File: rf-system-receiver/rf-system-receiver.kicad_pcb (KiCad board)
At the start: 4 copper layers, 53.3 x 51 mm, 55 parts, among them IC1 nRF905, J1 USB_B_Micro, J2 CONREVSMA001-G, J3 SWD, Q1 MMBT9013, SW1 SW_Push, U1 STM32F103C8Tx, U2 AMS1117-3.3, X1 16MHZ, X2 16MHZ

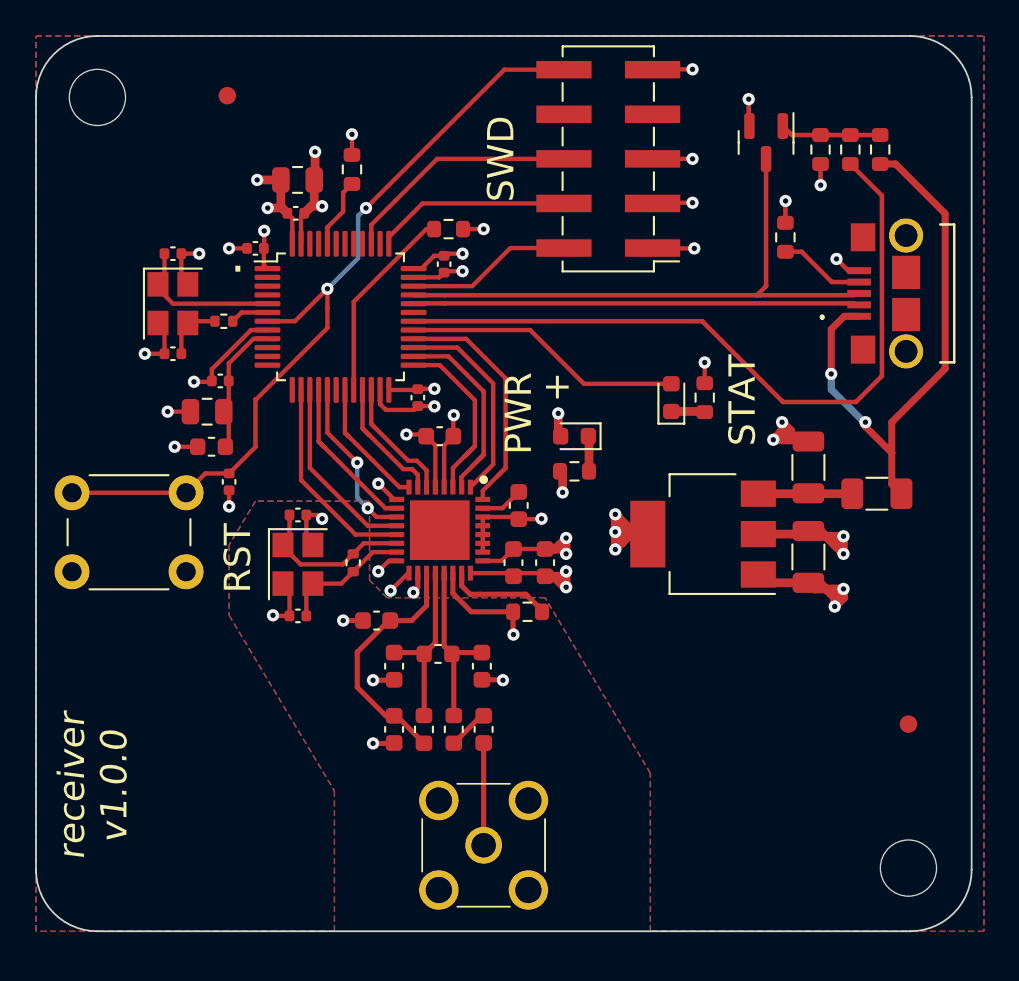
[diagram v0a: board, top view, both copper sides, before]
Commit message: add silkscreen, fiducials and tooling holes
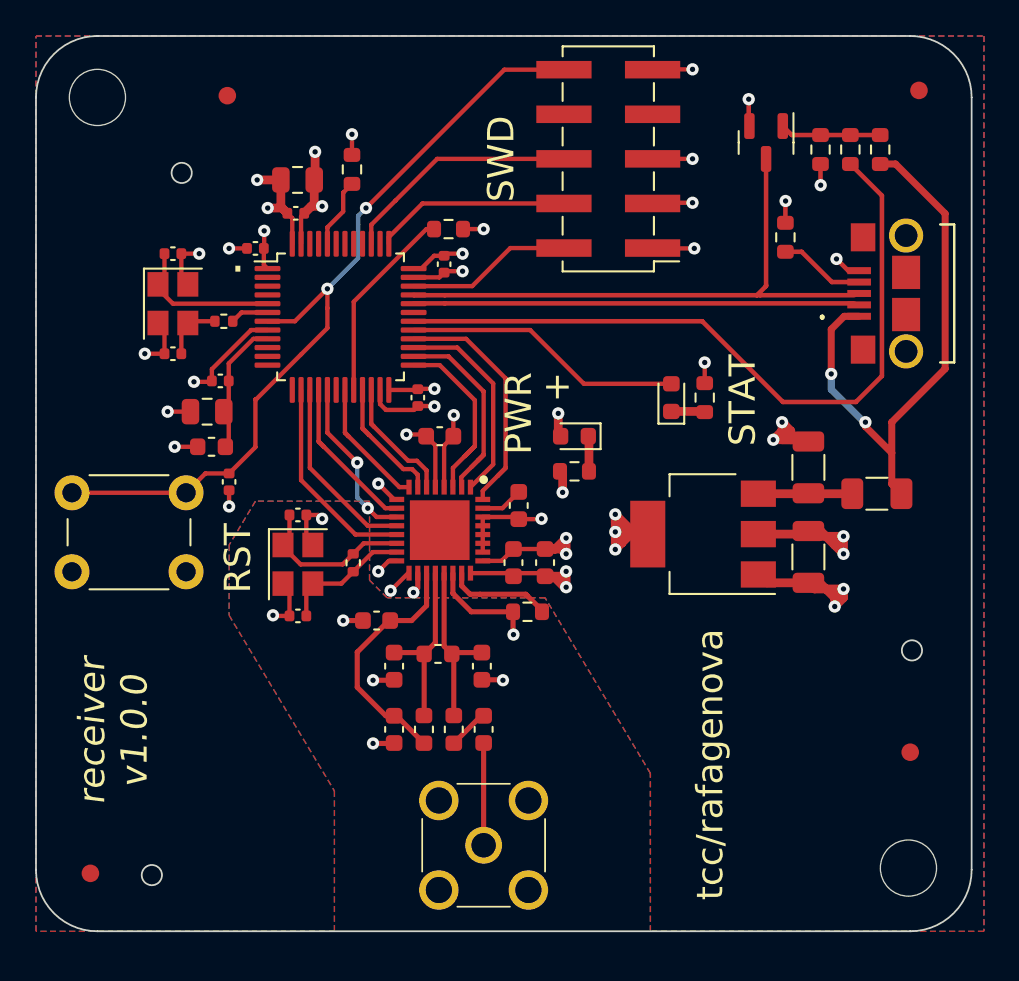
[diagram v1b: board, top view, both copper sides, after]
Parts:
- added FID3: Fiducial, Fiducial:Fiducial_1mm_Mask2mm, F.Cu at (119.1, 83.7)
- added FID4: Fiducial, Fiducial:Fiducial_1mm_Mask2mm, F.Cu at (166.3, 39.1)
- moved FID2 1.60 mm to (165.8, 76.8)
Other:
- outline, holes or cut-outs redrawn
- board text added: "tcc/rafagenova"
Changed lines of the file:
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@@
     )
+  )
+  (footprint "Fiducial:Fiducial_1mm_Mask2mm" (layer "F.Cu")
+    (at 166.3 39.1)
+    (descr "Circular Fiducial, 1mm bare copper, 2mm soldermask opening (Level A)")
+    (tags "fiducial")
+    (property "Sheetfile" "rf-system-receiver.kicad_sch")
+    (property "Sheetname" "")
+    (attr smd)
+    (fp_text reference "FID4" (at 0 -2) (layer "F.Fab")
+      (effects (font (size 1 1) (thickness 0.15)))
+    )
+    (fp_text value "Fiducial" (at 0 2) (layer "F.Fab")
+      (effects (font (size 1 1) (thickness 0.15)))
+    )
+    (fp_text user "${REFERENCE}" (at 0 0) (layer "F.Fab")
+      (effects (font (size 0.4 0.4) (thickness 0.06)))
+    )
+    (fp_circle (center 0 0) (end 1.25 0) (layer "F.CrtYd") (width 0.05) (fill none))
+    (fp_circle (center 0 0) (end 1 0) (layer "F.Fab") (width 0.1) (fill none))
+    (pad "" smd circle (at 0 0) (size 1 1) (layers "F.Cu" "F.Mask")
+      (solder_mask_margin 0.5) (clearance 0.5))
   )
   (footprint "Connector_PinHeader_2.54mm:PinHeader_2x05_P2.54mm_Vertical_SMD" (layer "F.Cu")
@@
   )
   (footprint "Fiducial:Fiducial_1mm_Mask2mm" (layer "F.Cu")
-    (at 165.7 75.2)
+    (at 165.8 76.8)
     (descr "Circular Fiducial, 1mm bare copper, 2mm soldermask opening (Level A)")
     (tags "fiducial")
@@
     )
   )
+  (footprint "Fiducial:Fiducial_1mm_Mask2mm" (layer "F.Cu")
+    (at 119.1 83.7)
+    (descr "Circular Fiducial, 1mm bare copper, 2mm soldermask opening (Level A)")
+    (tags "fiducial")
+    (property "Sheetfile" "rf-system-receiver.kicad_sch")
+    (property "Sheetname" "")
+    (attr smd)
+    (fp_text reference "FID3" (at 0 -2) (layer "F.Fab")
+      (effects (font (size 1 1) (thickness 0.15)))
+    )
+    (fp_text value "Fiducial" (at 0 2) (layer "F.Fab")
+      (effects (font (size 1 1) (thickness 0.15)))
+    )
+    (fp_text user "${REFERENCE}" (at 0 0) (layer "F.Fab")
+      (effects (font (size 0.4 0.4) (thickness 0.06)))
+    )
+    (fp_circle (center 0 0) (end 1.25 0) (layer "F.CrtYd") (width 0.05) (fill none))
+    (fp_circle (center 0 0) (end 1 0) (layer "F.Fab") (width 0.1) (fill none))
+    (pad "" smd circle (at 0 0) (size 1 1) (layers "F.Cu" "F.Mask")
+      (solder_mask_margin 0.5) (clearance 0.5))
+  )
   (footprint "Capacitor_SMD:C_0805_2012Metric" (layer "F.Cu")
     (at 125.75 57.4 180)
@@
   )
   (gr_line (start 119.5 87) (end 165.8 87) (layer "Edge.Cuts") (width 0.1))
+  (gr_circle (center 124.3 43.8) (end 124.876 43.8) (layer "Edge.Cuts") (width 0.1) (fill none))
   (gr_arc (start 116 39.5) (mid 117.025126 37.025126) (end 119.5 36) (layer "Edge.Cuts") (width 0.1))
+  (gr_circle (center 122.6 83.8) (end 123.176 83.8) (layer "Edge.Cuts") (width 0.1) (fill none))
   (gr_line (start 116 39.5) (end 116 83.5) (layer "Edge.Cuts") (width 0.1))
   (gr_arc (start 119.5 87) (mid 117.025126 85.974874) (end 116 83.5) (layer "Edge.Cuts") (width 0.1))
   (gr_arc (start 165.8 36) (mid 168.274874 37.025126) (end 169.3 39.5) (layer "Edge.Cuts") (width 0.1))
+  (gr_circle (center 165.9 71) (end 166.476 71) (layer "Edge.Cuts") (width 0.1) (fill none))
   (gr_line (start 165.8 36) (end 119.5 36) (layer "Edge.Cuts") (width 0.1))
   (gr_arc (start 169.3 83.5) (mid 168.274874 85.974874) (end 165.8 87) (layer "Edge.Cuts") (width 0.1))
@@
     (effects (font (size 1.5 1.5) (thickness 0.3)))
   )
-  (gr_text "receiver\nv1.0.0" (at 119.25 78.75 90) (layer "F.SilkS")
+  (gr_text "receiver\nv1.0.0" (at 120.4 75.6 90) (layer "F.SilkS")
     (effects (font (size 1.5 1.5) (thickness 0.3) italic))
   )
@@
     (effects (font (size 1.5 1.5) (thickness 0.3)))
   )
+  (gr_text "tcc/rafagenova" (at 154.4 77.5 90) (layer "F.SilkS")
+    (effects (font (size 1.5 1.5) (thickness 0.3)))
+  )

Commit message: adding LCSC Part # and small PCB modifs
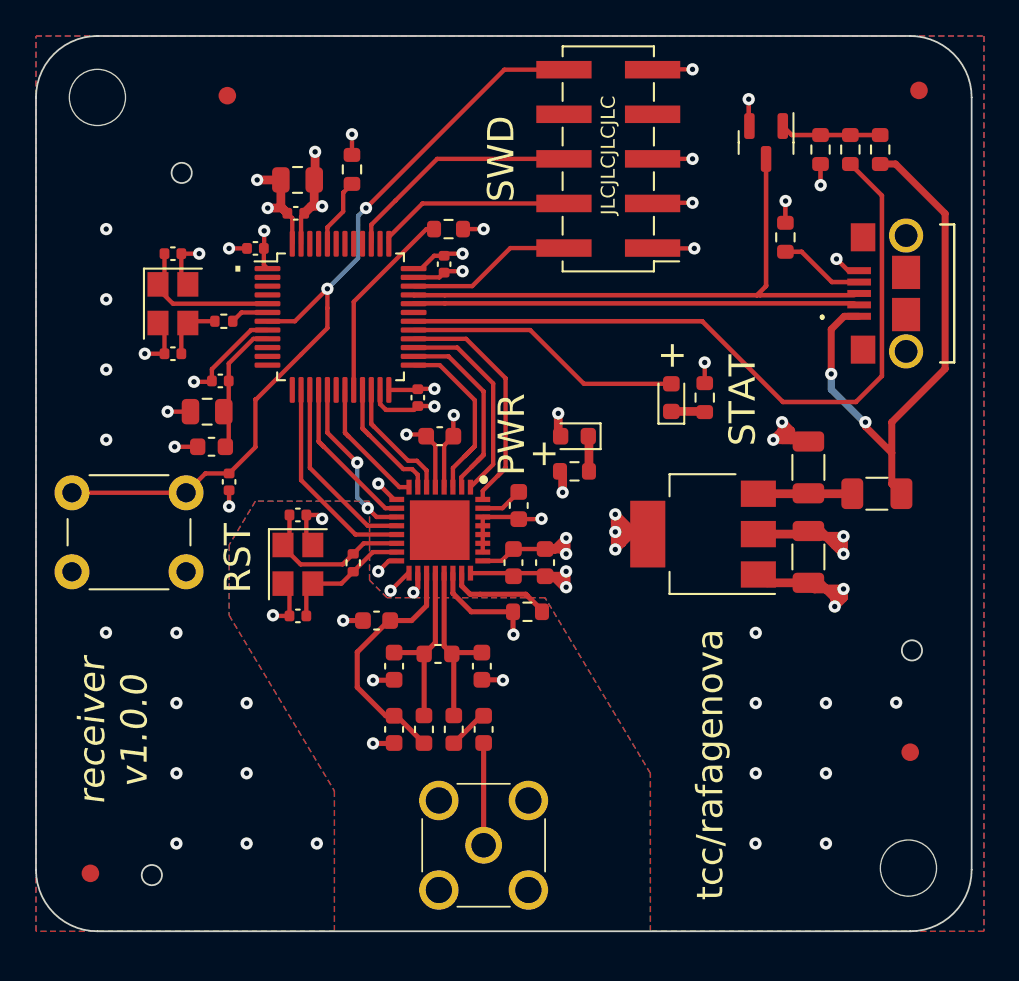
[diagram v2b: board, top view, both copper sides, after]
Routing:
- net GND: vias 38 -> 59
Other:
- board text added: "JLCJLCJLCJLC"
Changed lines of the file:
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@@
       (outputformat 1)
       (mirror false)
-      (drillshape 1)
+      (drillshape 0)
       (scaleselection 1)
-      (outputdirectory "")
+      (outputdirectory "gerber/")
     )
   )
@@
     (fp_line (start -1.6 0.8) (end -1.6 -0.8) (layer "F.Fab") (width 0.1))
     (fp_line (start -1.6 -0.8) (end 1.6 -0.8) (layer "F.Fab") (width 0.1))
-    (pad "1" smd roundrect (at -1.475 0 270) (size 1.15 1.8) (layers "F.Cu" "F.Paste" "F.Mask") (roundrect_rratio 0.217391)
+    (pad "1" smd roundrect (at -1.475 0 270) (size 1.15 1.8) (layers "F.Cu" "F.Paste" "F.Mask") (roundrect_rratio 0.2173913043)
       (net 2 "+3V3") (pintype "passive"))
-    (pad "2" smd roundrect (at 1.475 0 270) (size 1.15 1.8) (layers "F.Cu" "F.Paste" "F.Mask") (roundrect_rratio 0.217391)
+    (pad "2" smd roundrect (at 1.475 0 270) (size 1.15 1.8) (layers "F.Cu" "F.Paste" "F.Mask") (roundrect_rratio 0.2173913043)
       (net 1 "GND") (pintype "passive"))
     (model "${KICAD6_3DMODEL_DIR}/Capacitor_SMD.3dshapes/C_1206_3216Metric.wrl"
@@
     (fp_line (start -1.6 0.8) (end -1.6 -0.8) (layer "F.Fab") (width 0.1))
     (fp_line (start 1.6 -0.8) (end 1.6 0.8) (layer "F.Fab") (width 0.1))
-    (pad "1" smd roundrect (at -1.475 0 90) (size 1.15 1.8) (layers "F.Cu" "F.Paste" "F.Mask") (roundrect_rratio 0.217391)
+    (pad "1" smd roundrect (at -1.475 0 90) (size 1.15 1.8) (layers "F.Cu" "F.Paste" "F.Mask") (roundrect_rratio 0.2173913043)
       (net 3 "Net-(C2-Pad1)") (pintype "passive"))
-    (pad "2" smd roundrect (at 1.475 0 90) (size 1.15 1.8) (layers "F.Cu" "F.Paste" "F.Mask") (roundrect_rratio 0.217391)
+    (pad "2" smd roundrect (at 1.475 0 90) (size 1.15 1.8) (layers "F.Cu" "F.Paste" "F.Mask") (roundrect_rratio 0.2173913043)
       (net 1 "GND") (pintype "passive"))
     (model "${KICAD6_3DMODEL_DIR}/Capacitor_SMD.3dshapes/C_1206_3216Metric.wrl"
@@
   (gr_arc (start 169.3 83.5) (mid 168.274874 85.974874) (end 165.8 87) (layer "Edge.Cuts") (width 0.1))
   (gr_line (start 169.3 83.5) (end 169.3 39.5) (layer "Edge.Cuts") (width 0.1))
-  (gr_text "PWR" (at 143.5 57.5 90) (layer "F.SilkS")
+  (gr_text "+" (at 152.3 54.2 270) (layer "F.SilkS")
+    (effects (font (size 1.5 1.5) (thickness 0.3)))
+  )
+  (gr_text "PWR" (at 143.1 58.7 90) (layer "F.SilkS")
     (effects (font (size 1.5 1.5) (thickness 0.3)))
   )
@@
     (effects (font (size 1.5 1.5) (thickness 0.3)))
   )
-  (gr_text "+" (at 145.75 56 270) (layer "F.SilkS")
+  (gr_text "+" (at 145 59.8 270) (layer "F.SilkS")
     (effects (font (size 1.5 1.5) (thickness 0.3)))
+  )
+  (gr_text "JLCJLCJLCJLC" (at 148.6 42.8 90) (layer "F.SilkS")
+    (effects (font (size 0.8 0.8) (thickness 0.15)))
   )
   (gr_text "tcc/rafagenova" (at 154.4 77.5 90) (layer "F.SilkS")
@@
   (segment (start 158.69 45.41) (end 158.7 45.4) (width 0.261112) (layer "F.Cu") (net 1))
   (via (at 137.1 58.7) (size 0.7) (drill 0.3) (layers "F.Cu" "B.Cu") (free) (net 1))
+  (via (at 120 55) (size 0.7) (drill 0.3) (layers "F.Cu" "B.Cu") (free) (net 1))
   (via (at 146 62) (size 0.7) (drill 0.3) (layers "F.Cu" "B.Cu") (free) (net 1))
   (via (at 158.5 58) (size 0.7) (drill 0.3) (layers "F.Cu" "B.Cu") (free) (net 1))
@@
   (via (at 132.3 63.5) (size 0.7) (drill 0.3) (layers "F.Cu" "B.Cu") (free) (net 1))
   (via (at 153.4 45.5) (size 0.7) (drill 0.3) (layers "F.Cu" "B.Cu") (net 1))
+  (via (at 157 70) (size 0.7) (drill 0.3) (layers "F.Cu" "B.Cu") (free) (net 1))
+  (via (at 123.999999 82) (size 0.7) (drill 0.3) (layers "F.Cu" "B.Cu") (free) (net 1))
   (via (at 140.3 49.4) (size 0.7) (drill 0.3) (layers "F.Cu" "B.Cu") (free) (net 1))
   (via (at 146.2 66.5) (size 0.7) (drill 0.3) (layers "F.Cu" "B.Cu") (free) (net 1))
   (via (at 129.5 69) (size 0.7) (drill 0.3) (layers "F.Cu" "B.Cu") (free) (net 1))
+  (via (at 120 47) (size 0.7) (drill 0.3) (layers "F.Cu" "B.Cu") (free) (net 1))
   (via (at 137.5 67.7) (size 0.7) (drill 0.3) (layers "F.Cu" "B.Cu") (free) (net 1))
   (via (at 133.5 69.3) (size 0.7) (drill 0.3) (layers "F.Cu" "B.Cu") (free) (net 1))
   (via (at 160.7 44.5) (size 0.7) (drill 0.3) (layers "F.Cu" "B.Cu") (free) (net 1))
   (via (at 125.3 48.4) (size 0.7) (drill 0.3) (layers "F.Cu" "B.Cu") (free) (net 1))
+  (via (at 157 78) (size 0.7) (drill 0.3) (layers "F.Cu" "B.Cu") (free) (net 1))
   (via (at 122.2 54.1) (size 0.7) (drill 0.3) (layers "F.Cu" "B.Cu") (free) (net 1))
+  (via (at 157 74) (size 0.7) (drill 0.3) (layers "F.Cu" "B.Cu") (free) (net 1))
+  (via (at 120 59) (size 0.7) (drill 0.3) (layers "F.Cu" "B.Cu") (free) (net 1))
   (via (at 135.5 66.5) (size 0.7) (drill 0.3) (layers "F.Cu" "B.Cu") (free) (net 1))
   (via (at 134 41.6) (size 0.7) (drill 0.3) (layers "F.Cu" "B.Cu") (free) (net 1))
   (via (at 162 67.5) (size 0.7) (drill 0.3) (layers "F.Cu" "B.Cu") (free) (net 1))
+  (via (at 123.999055 74) (size 0.7) (drill 0.3) (layers "F.Cu" "B.Cu") (free) (net 1))
+  (via (at 120 51) (size 0.7) (drill 0.3) (layers "F.Cu" "B.Cu") (free) (net 1))
+  (via (at 124 78) (size 0.7) (drill 0.3) (layers "F.Cu" "B.Cu") (free) (net 1))
+  (via (at 161 82) (size 0.7) (drill 0.3) (layers "F.Cu" "B.Cu") (free) (net 1))
+  (via (at 156.987016 82) (size 0.7) (drill 0.3) (layers "F.Cu" "B.Cu") (free) (net 1))
+  (via (at 161 74) (size 0.7) (drill 0.3) (layers "F.Cu" "B.Cu") (free) (net 1))
   (via (at 143.2 70.1) (size 0.7) (drill 0.3) (layers "F.Cu" "B.Cu") (free) (net 1))
   (via (at 142.6 72.7) (size 0.7) (drill 0.3) (layers "F.Cu" "B.Cu") (free) (net 1))
+  (via (at 165 73.974032) (size 0.7) (drill 0.3) (layers "F.Cu" "B.Cu") (free) (net 1))
   (via (at 132.3 45.7) (size 0.7) (drill 0.3) (layers "F.Cu" "B.Cu") (free) (net 1))
+  (via (at 128 78) (size 0.7) (drill 0.3) (layers "F.Cu" "B.Cu") (free) (net 1))
   (via (at 131.9 42.6) (size 0.7) (drill 0.3) (layers "F.Cu" "B.Cu") (free) (net 1))
   (via (at 158 59) (size 0.7) (drill 0.3) (layers "F.Cu" "B.Cu") (free) (net 1))
+  (via (at 119.987016 69.987016) (size 0.7) (drill 0.3) (layers "F.Cu" "B.Cu") (free) (net 1))
   (via (at 144.8 63.5) (size 0.7) (drill 0.3) (layers "F.Cu" "B.Cu") (free) (net 1))
+  (via (at 132 82) (size 0.7) (drill 0.3) (layers "F.Cu" "B.Cu") (free) (net 1))
   (via (at 135.2 76.3) (size 0.7) (drill 0.3) (layers "F.Cu" "B.Cu") (free) (net 1))
   (via (at 135.5 61.5) (size 0.7) (drill 0.3) (layers "F.Cu" "B.Cu") (free) (net 1))
   (via (at 154.09375 54.6) (size 0.7) (drill 0.3) (layers "F.Cu" "B.Cu") (free) (net 1))
   (via (at 125 55.7) (size 0.7) (drill 0.3) (layers "F.Cu" "B.Cu") (free) (net 1))
+  (via (at 161 78) (size 0.7) (drill 0.3) (layers "F.Cu" "B.Cu") (free) (net 1))
   (via (at 153.4 37.9) (size 0.7) (drill 0.3) (layers "F.Cu" "B.Cu") (net 1))
   (via (at 146.2 67.4) (size 0.7) (drill 0.3) (layers "F.Cu" "B.Cu") (free) (net 1))
   (via (at 127 48.1) (size 0.7) (drill 0.3) (layers "F.Cu" "B.Cu") (free) (net 1))
   (via (at 153.4 43) (size 0.7) (drill 0.3) (layers "F.Cu" "B.Cu") (net 1))
+  (via (at 128 74) (size 0.7) (drill 0.3) (layers "F.Cu" "B.Cu") (free) (net 1))
   (via (at 141.5 47) (size 0.7) (drill 0.3) (layers "F.Cu" "B.Cu") (free) (net 1))
   (via (at 123.5 57.4) (size 0.7) (drill 0.3) (layers "F.Cu" "B.Cu") (free) (net 1))
@@
   (via (at 127 62.8) (size 0.7) (drill 0.3) (layers "F.Cu" "B.Cu") (free) (net 1))
   (via (at 161.6 48.7) (size 0.7) (drill 0.3) (layers "F.Cu" "B.Cu") (net 1))
+  (via (at 124 70) (size 0.7) (drill 0.3) (layers "F.Cu" "B.Cu") (free) (net 1))
+  (via (at 128 82) (size 0.7) (drill 0.3) (layers "F.Cu" "B.Cu") (free) (net 1))
   (via (at 161.5 68.5) (size 0.7) (drill 0.3) (layers "F.Cu" "B.Cu") (free) (net 1))
   (segment (start 130.02 45.8) (end 130.32 46.1) (width 0.5) (layer "F.Cu") (net 2))
